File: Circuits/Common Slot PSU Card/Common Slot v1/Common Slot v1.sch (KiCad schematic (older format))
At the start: 59 parts, among them J1 32x2P Card Edge, J10 A1, J11 A2, J12 +12V, J13 0V, J14 +12V, J15 +12V, J16 +12V, J17 0V, J18 0V, J19 0V, J2 ENj, J20 +12V, J21 +12V, J22 +12V, J23 +12V, J24 0V, J25 0V, J26 0V, J27 0V, J28 +12V, J29 +12V, J3 ENi, J30 +12V, J31 +12V, J32 0V, J33 0V, J34 0V, J35 0V, J36 +12V, J37 +12V, J38 +12V, J39 0V, J4 µMolex, J40 0V, J41 0V, J42 +12V, J43 +12V, J44 0V, J45 0V, J5 5Vsb, J6 12Vsb, J7 Vdisplay, J8 I2C, J9 A0, SW1 ENsw, U1 LTV-817, U2 L7805

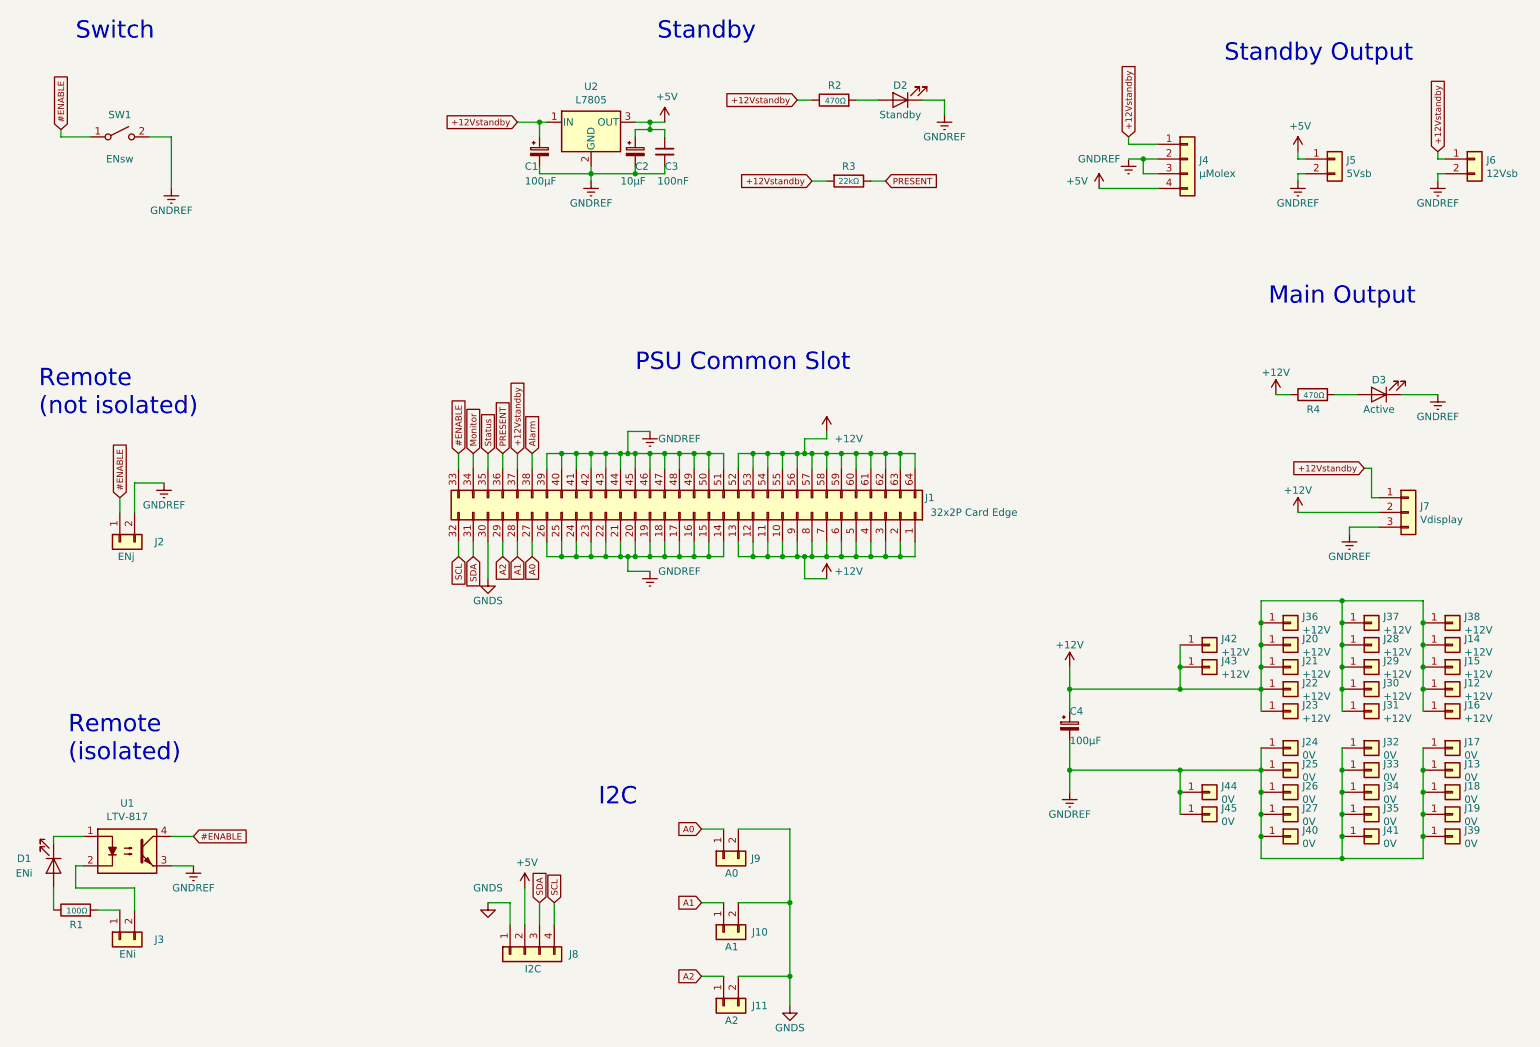
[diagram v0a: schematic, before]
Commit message: PSU Breakout: Arranging in mini form factor
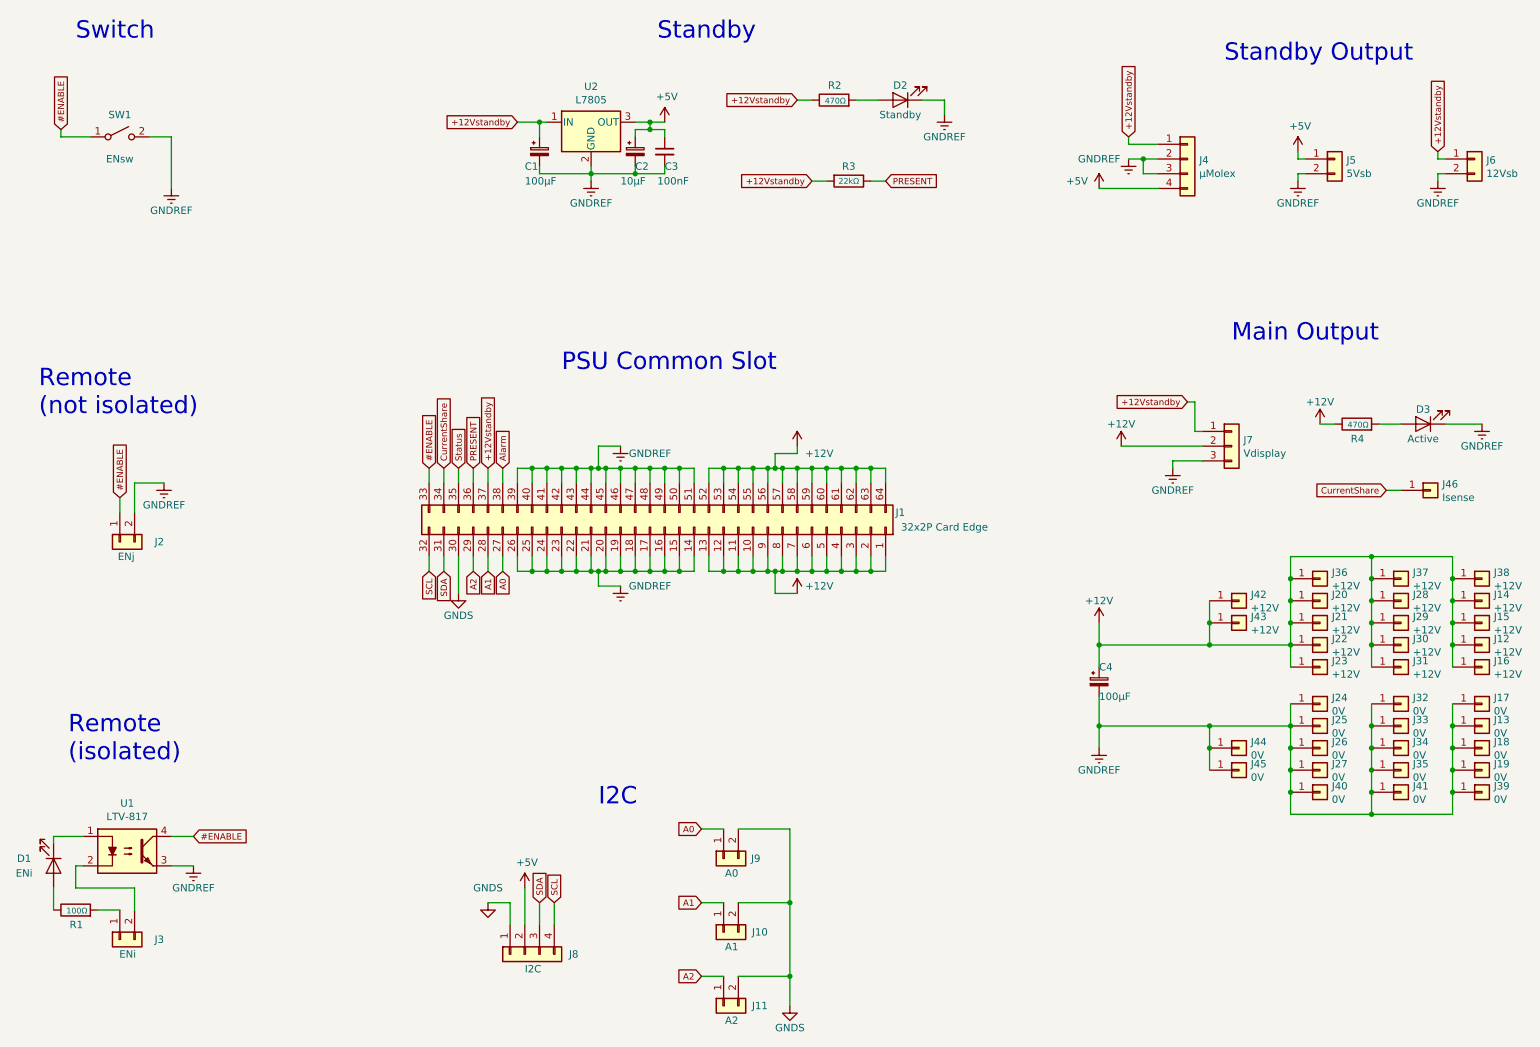
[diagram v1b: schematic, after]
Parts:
- added J46: Isense, Footprints:WIRE-16AWG, symbol conn:Conn_01x01
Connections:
- net Monitor renamed CurrentShare
- net CurrentShare: now also J46.1 (Pin_1)
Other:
- moved on the sheet: C4, D3, J1, J12, J13, J14, J15, J16, J17, J18, J19, J20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
